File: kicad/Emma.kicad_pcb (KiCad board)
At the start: 4 copper layers, 55 x 35 mm, 75 parts, among them U1 ByA 100nF +3V3 U1-VDDA Bypass, U1 ByB 100nF +3V3 U1-VDD Bypass

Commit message: Fix 49 MHz Emma link regulatory citation: Part 95 RCRS -> Part 15 §15.235
Part 95 Subpart C (Radio Control Radio Service) covers only 26-28 MHz,
72 MHz, and 75 MHz -- it has no provisions for 49 MHz. The 49.82-49.90 MHz
band Emma actually uses is governed by 47 CFR Part 15 §15.235, an
unlicensed intentional-radiator rule with a field-strength limit, not a
licensed/license-exempt personal radio service.

Also corrects a previously-unnoticed downstream consequence: §15.235's
10,000 µV/m-at-3m field-strength limit converts to an EIRP ceiling of
only ~30 µW (-15.2 dBm), about 35 dB below the 100 mW the project's
antenna/power budget assumed. malcolm_antenna_spec.md, Emma.md, and
REFERENCES.md now document the true ceiling and flag the link as
severely range-limited; TODO.md §0.1 tracks the required PA/range
re-architecture as a separate, deferred item (no frequency or hardware
change made in this pass). Also flags a confirmed §15.203
antenna-connector gap (Emma uses a standard SMA jack).

Updates citations across REFERENCES.md, CLAUDE.md, TODO.md, README.md,
PROJECT_INDEX.md, KiCad schematic/PCB silkscreen text and source
generator, firmware comments, and build docs. Internal naming
conventions ("RCRS-49" module name, file names, code symbols) are left
unchanged -- only regulatory citations and compliance prose are
corrected. Also fixes an unrelated wrong citation found in passing
(SiK 915 MHz mis-cited as Part 97 Amateur Radio Service).

Co-Authored-By: Claude Sonnet 4.6 <noreply@anthropic.com>
Claude-Session: https://claude.ai/code/session_014uXbK3iF9VFoBsweHtxGJL
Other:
- board text added: "49 MHz AX.25 KISS Transceiver XCVR-49MHZ-2 Rev 2 — EMI-Hardened FCC 47 CFR Part 15 15.235 49.830-49.890 MHz AFSK 1200bd CC BY 4.0 — June 2026 Steve Griffing PE(CSE), CISSP-ISSEP, CPP Griffing Technology LLC github.com/Stab-Rabbit-Coding"
- board text removed: "49 MHz AX.25 KISS Transceiver XCVR-49MHZ-2 Rev 2 — EMI-Hardened FCC Part 95 Subpart D 49.830-49.890 MHz AFSK 1200bd CC BY 4.0 — June 2026 Steve Griffing PE(CSE), CISSP-ISSEP, CPP Griffing Technology LLC github.com/Stab-Rabbit-Coding"
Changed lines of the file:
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@@
 		(comment 1 "Serenity-Class Tiltrotor UAV — 49 MHz AX.25 RCRS Transceiver Module Rev 2")
 		(comment 2 "CC BY 4.0 creativecommons.org/licenses/by/4.0 — Steve Griffing PE(CSE) CISSP-ISSEP CPP")
-		(comment 3 "55x35mm 4L JLCPCB — FCC Part 95 Subpart D — 49.830–49.890 MHz AFSK 1200bd AX.25")
+		(comment 3 "55x35mm 4L JLCPCB — FCC 47 CFR Part 15 15.235 — 49.830–49.890 MHz AFSK 1200bd AX.25")
 		(comment 4 "EMI hardening: SRF2012 CMC + PRTR5V0U2X TVS + Wuerth 742792512 FB + X2Y 4.7nF cap")
 		(comment 5 "Hull: misubisu CC BY 4.0 | Firefly/Serenity fan-work, not officially licensed")
@@
 		)
 	)
-	(gr_text "49 MHz AX.25 KISS Transceiver\nXCVR-49MHZ-2 Rev 2 — EMI-Hardened\nFCC Part 95 Subpart D\n49.830-49.890 MHz  AFSK 1200bd\nCC BY 4.0 — June 2026\nSteve Griffing\nPE(CSE), CISSP-ISSEP, CPP\nGriffing Technology LLC\ngithub.com/Stab-Rabbit-Coding"
+	(gr_text "49 MHz AX.25 KISS Transceiver\nXCVR-49MHZ-2 Rev 2 — EMI-Hardened\nFCC 47 CFR Part 15 15.235\n49.830-49.890 MHz  AFSK 1200bd\nCC BY 4.0 — June 2026\nSteve Griffing\nPE(CSE), CISSP-ISSEP, CPP\nGriffing Technology LLC\ngithub.com/Stab-Rabbit-Coding"
 		(at 142.5 116.5 270)
 		(layer "B.SilkS")

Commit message: Resolve Emma 49 MHz §15.203 connector violation with RP-SMA
J2 changed from a standard SMA edge jack (Amphenol 132289) to its
reverse-polarity counterpart (Amphenol 132289RP) -- identical PCB
footprint, reversed mating-pin gender -- so generic standard-SMA
antennas/cables cannot mechanically connect, satisfying 47 CFR
§15.203's "unique coupling" provision for intentional radiators.

Updates Emma.kicad_sch (lib symbol + J2 instance Value/Description),
Emma.kicad_pcb (footprint Value/Description properties, ANT silkscreen
label, ESD note), Emma.md, and the Malcolm GCS wiring/antenna-spec docs
that mirror Emma's connector on the ground station side. REFERENCES.md
and TODO.md updated from "open violation" to "resolved in design,
board re-spin pending" status.

KiCad CLI is unavailable in this environment so DRC could not be
re-run; changes are limited to text properties/silkscreen labels with
no net, pad, or geometry changes, so no DRC impact is expected.

Co-Authored-By: Claude Sonnet 4.6 <noreply@anthropic.com>
Claude-Session: https://claude.ai/code/session_014uXbK3iF9VFoBsweHtxGJL
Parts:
- ANT RPSMA: renamed from ANT SMA; value SMA-EDGE-50R -> RPSMA-EDGE-50R
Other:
- board text added: "J2 RP-SMA"
- board text removed: "J2 SMA"
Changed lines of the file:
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@@
 		(layer "F.Cu")
 		(at 152.5 112.46)
-		(property "Reference" "ANT SMA"
+		(property "Reference" "ANT RPSMA"
 			(at -2.5 -6.5 0)
 			(layer "F.SilkS")
@@
 			)
 		)
-		(property "Value" "SMA-EDGE-50R"
+		(property "Value" "RPSMA-EDGE-50R"
 			(at 7.5 0 90)
 			(layer "F.Fab")
@@
 			)
 		)
-		(property "Description" "SMA edge-mount 50 Ω antenna connector — 49 MHz ANT"
+		(property "Description" "RP-SMA edge-mount 50 Ω antenna connector (Amphenol 132289RP) — 49 MHz ANT — 47 CFR Part 15 15.203 unique-coupling antenna restriction"
 			(at 35 0 270)
 			(layer "F.Fab")
@@
 			)
 		)
-		(property "Description" "NXP PRTR5V0U2X dual TVS 5V SOT-363 — ESD protection near SMA J2"
+		(property "Description" "NXP PRTR5V0U2X dual TVS 5V SOT-363 — ESD protection near RP-SMA J2"
 			(at 1.5 -21.5 0)
 			(layer "F.Fab")
@@
 		)
 	)
-	(gr_text "J2 SMA"
+	(gr_text "J2 RP-SMA"
 		(at 149.6 114.5 0)
 		(layer "F.Fab")

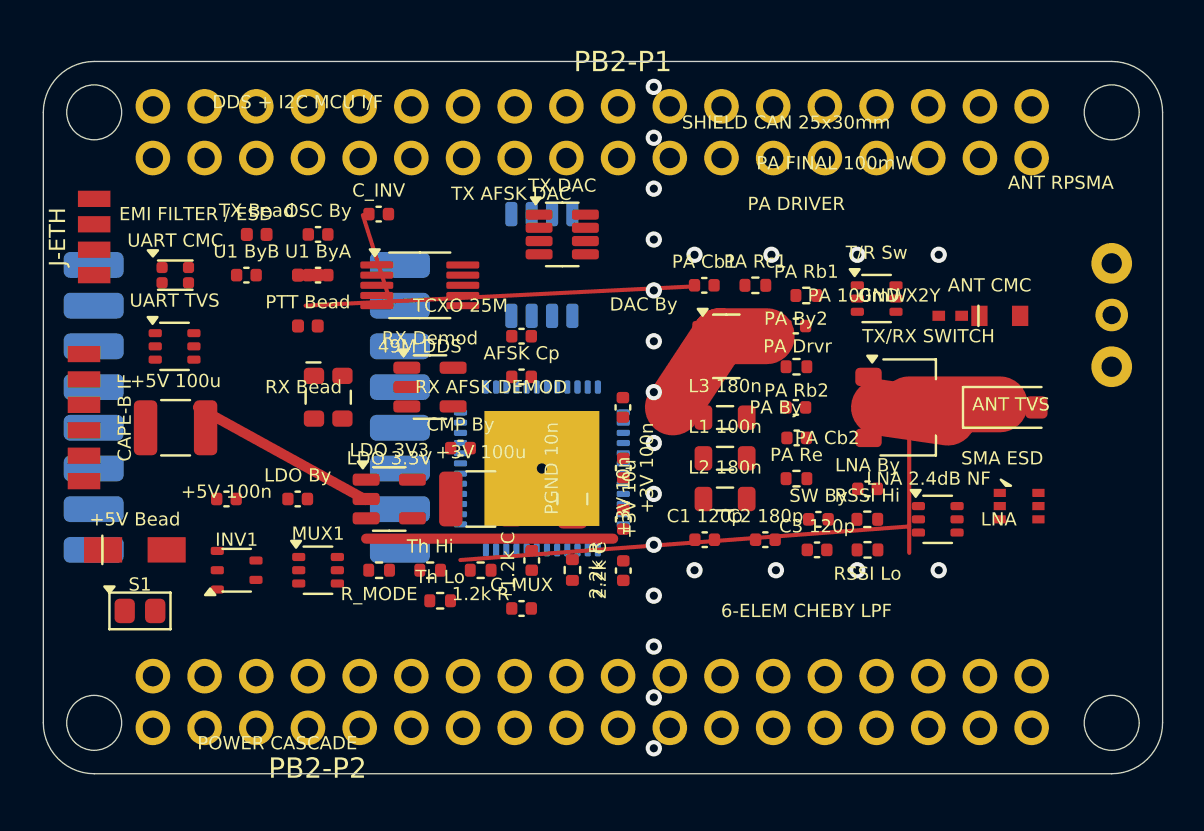
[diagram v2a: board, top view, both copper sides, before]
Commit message: Fix Emma ERC/DRC errors: schematic parser crash, J1 pin mirroring, 12 PCB shorts
Schematic (Emma.kicad_sch):
- Remove stray ;; comment that silently broke KiCad's S-expr parser,
  causing ERC to fail to load the file entirely (CLAUDE.md prohibits ;/#
  comments in KiCad files for exactly this reason).
- Fix Conn_JST_GH_06P pin Y-offset sign: J1's SHIELD/MP pin and all six
  numbered pins were mirrored relative to where their wires/power symbols
  were actually drawn, leaving the PGND bond and J1 unconnected.
- Add PWR_FLAG markers on the J1 GND/+5V/PGND nets to silence the
  power-pin-not-driven check (standard KiCad mechanism for sub-circuit
  schematics with no local power source).
- Fix FB1 wire endpoint that stopped 3.81mm short of the real pin.
ERC: 0 errors (was: file failed to load).

PCB (Emma.kicad_pcb):
- Fix 4 track segments with erroneous 2.75mm width (RF_TX, GND) that
  caused them to physically overlap nearby vias/pads despite reasonable
  centerline routing; corrected to 0.2mm/0.5mm matching established
  nets in the same area.
- Remove 3 orphaned copper stubs (TCXO_OUT, one GND stitch, one more GND
  stitch) that didn't connect to any real pad at either end and were
  shorting against unrelated nets they merely passed near.
- Reroute DDS_RF around the 49M DDS pin columns, the GND via-stitch
  fence at x=130, and neighboring components (+3V 10u, U1 ByA) instead
  of cutting through them.
- Nudge the two end vias of the x=130 GND stitching fence by 0.25mm
  (134.0/103.5 instead of 133.75/103.75) to clear PB2-P1/P2 hole
  clearance; fence interior pitch (2.5mm, 12 gaps) unchanged.
DRC: shorting_items/tracks_crossing/courtyards_overlap/hole_clearance
all at 0 (was 12/1/1/2 respectively).

Co-Authored-By: Claude Sonnet 4.6 <noreply@anthropic.com>
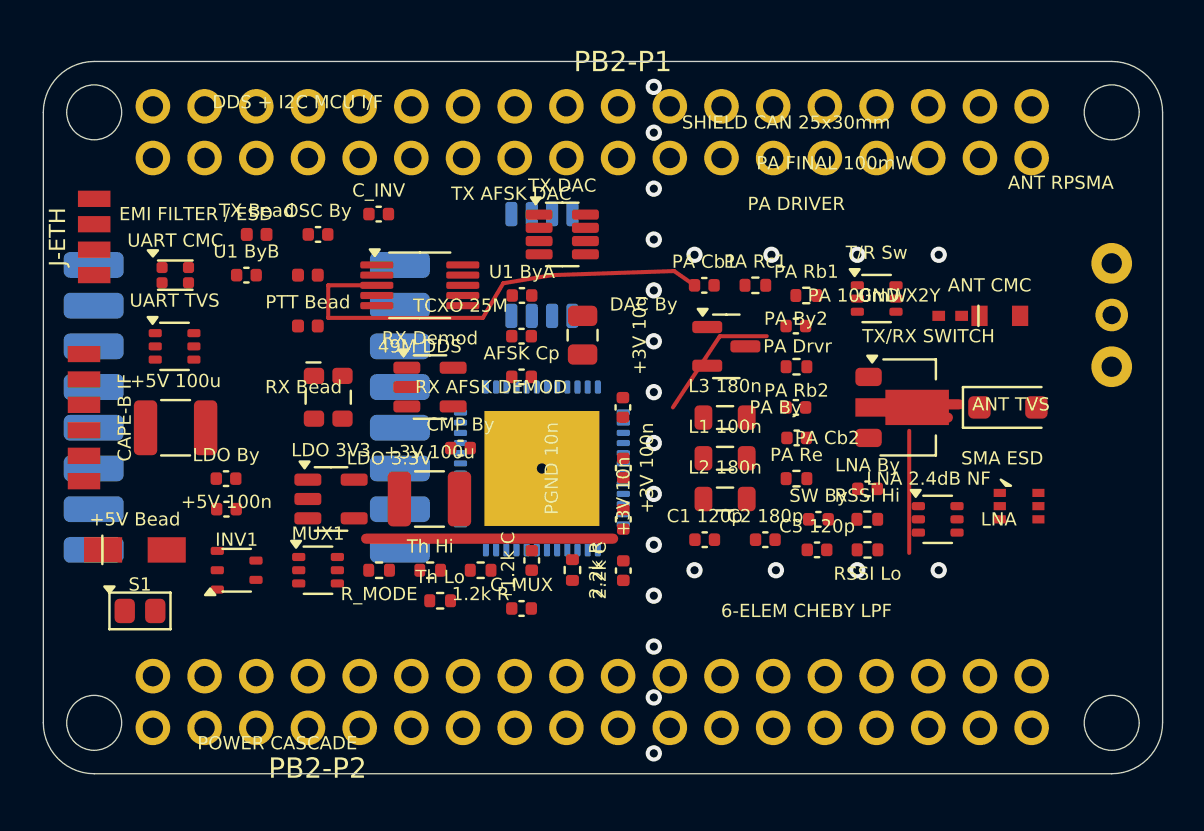
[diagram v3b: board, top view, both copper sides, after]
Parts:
- moved U1 ByA 10.1 mm to (123.5, 111.5)
- moved +3V 10u 8.07 mm to (126.5, 113.5)
- moved LDO By 3.66 mm to (109.0, 120.5)
- moved LDO 3V3 2.86 mm to (114.1, 121.5)
- moved +3V 100u 2.53 mm to (119.0, 121.5)
- moved +5V 100n 0.50 mm to (109.0, 122.0)
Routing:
- net GND: track 57.6 -> 30.5 mm
- net RF_TX: track 6.50 -> 0.00 mm
- net TCXO_OUT: track 4.67 -> 0.00 mm
- net DDS_RF: track 19.2 -> 23.2 mm
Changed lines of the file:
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@@
 	(footprint "C_0402_1005Metric"
 		(layer "F.Cu")
-		(at 112.5 121.5)
+		(at 108.98 120.5)
 		(descr "Capacitor SMD 0402 (1005 Metric), square (rectangular) end terminal, IPC-7351 nominal, (Body size source: IPC-SM-782 page 76, https://www.pcb-3d.com/wordpress/wp-content/uploads/ipc-sm-782a_amendment_1_and_2.pdf), generated with kicad-footprint-generator")
 		(tags "capacitor")
@@
 	(footprint "C_1210_3225Metric"
 		(layer "F.Cu")
-		(at 121.5 121.5)
+		(at 118.975 121.5)
 		(descr "Capacitor SMD 1210 (3225 Metric), square (rectangular) end terminal, IPC-7351 nominal, (Body size source: IPC-SM-782 page 76, https://www.pcb-3d.com/wordpress/wp-content/uploads/ipc-sm-782a_amendment_1_and_2.pdf), generated with kicad-footprint-generator")
 		(tags "capacitor")
@@
 	(footprint "C_0805_2012Metric"
 		(layer "F.Cu")
-		(at 126 121.5 -90)
+		(at 126.5 113.45 -90)
 		(descr "Capacitor SMD 0805 (2012 Metric), square (rectangular) end terminal, IPC-7351 nominal, (Body size source: IPC-SM-782 page 76, https://www.pcb-3d.com/wordpress/wp-content/uploads/ipc-sm-782a_amendment_1_and_2.pdf, https://docs.google.com/spreadsheets/d/1BsfQQcO9C6DZCsRaXUlFlo91Tg2WpOkGARC1WS5S8t0/edit?usp=sharing), generated with kicad-footprint-generator")
 		(tags "capacitor")
@@
 	(footprint "C_0402_1005Metric"
 		(layer "F.Cu")
-		(at 113.5 110.5)
+		(at 123.52 111.5)
 		(descr "Capacitor SMD 0402 (1005 Metric), square (rectangular) end terminal, IPC-7351 nominal, (Body size source: IPC-SM-782 page 76, https://www.pcb-3d.com/wordpress/wp-content/uploads/ipc-sm-782a_amendment_1_and_2.pdf), generated with kicad-footprint-generator")
 		(tags "capacitor")
@@
 	(footprint "C_0402_1005Metric"
 		(layer "F.Cu")
-		(at 109 121.5)
+		(at 109 122)
 		(descr "Capacitor SMD 0402 (1005 Metric), square (rectangular) end terminal, IPC-7351 nominal, (Body size source: IPC-SM-782 page 76, https://www.pcb-3d.com/wordpress/wp-content/uploads/ipc-sm-782a_amendment_1_and_2.pdf), generated with kicad-footprint-generator")
 		(tags "capacitor")
@@
 	(footprint "SOT-23-5"
 		(layer "F.Cu")
-		(at 117 121.5)
+		(at 114.1375 121.5)
 		(descr "SOT, 5 Pin (JEDEC MO-178 Var AA https://www.jedec.org/document_search?search_api_views_fulltext=MO-178), generated with kicad-footprint-generator ipc_gullwing_generator.py")
 		(tags "SOT TO_SOT_SMD")
@@
 	)
 	(segment
-		(start 141.0625 117)
-		(end 144.45 117.5)
-		(width 2.75)
+		(start 135.55 113.5)
+		(end 133.24375 113.5)
+		(width 0.2)
 		(layer "F.Cu")
 		(net 1)
 	)
 	(segment
-		(start 142.55 116.85)
-		(end 147 116.85)
-		(width 2.75)
+		(start 141.0625 117)
+		(end 144.45 117.5)
+		(width 0.5)
 		(layer "F.Cu")
 		(net 1)
 	)
 	(segment
-		(start 107.6 117)
-		(end 115.8625 121.55)
+		(start 142.55 116.85)
+		(end 145 116.85)
 		(width 0.5)
 		(layer "F.Cu")
@@
 	)
 	(segment
-		(start 142.55 122.85)
-		(end 120.49 124.5)
+		(start 133.24375 113.5)
+		(end 130.9375 117)
 		(width 0.2)
 		(layer "F.Cu")
@@
 	)
 	(via
-		(at 130 133.75)
+		(at 130 134.0)
 		(size 0.8)
 		(drill 0.4)
@@
 	)
 	(via
-		(at 130 103.75)
+		(at 130 103.5)
 		(size 0.8)
 		(drill 0.4)
@@
 		(net 1)
 	)
-	(segment
-		(start 135.55 113.5)
-		(end 133.24375 113.5)
-		(width 2.75)
-		(layer "F.Cu")
-		(net 8)
-	)
-	(segment
-		(start 133.24375 113.5)
-		(end 130.9375 117)
-		(width 2.75)
-		(layer "F.Cu")
-		(net 8)
-	)
 	(via
 		(at 130 108.75)
@@
 	)
 	(segment
-		(start 112.8875 112)
-		(end 132.0625 111.05)
+		(start 116.3875 111.0)
+		(end 114.0 111.0)
+		(width 0.2)
+		(layer "F.Cu")
+		(net 17)
+	)
+	(segment
+		(start 114.0 111.0)
+		(end 114.0 112.6)
+		(width 0.2)
+		(layer "F.Cu")
+		(net 17)
+	)
+	(segment
+		(start 114.0 112.6)
+		(end 121.6 112.6)
+		(width 0.2)
+		(layer "F.Cu")
+		(net 17)
+	)
+	(segment
+		(start 121.6 112.6)
+		(end 122.6 110.9)
+		(width 0.2)
+		(layer "F.Cu")
+		(net 17)
+	)
+	(segment
+		(start 122.6 110.9)
+		(end 125.0 110.5)
+		(width 0.2)
+		(layer "F.Cu")
+		(net 17)
+	)
+	(segment
+		(start 125.0 110.5)
+		(end 131.0 110.3)
+		(width 0.2)
+		(layer "F.Cu")
+		(net 17)
+	)
+	(segment
+		(start 131.0 110.3)
+		(end 132.0 111.0)
 		(width 0.2)
 		(layer "F.Cu")
@@
 		(net 18)
 	)
-	(segment
-		(start 115.7 107.55)
-		(end 117.1125 112)
-		(width 0.2)
-		(layer "F.Cu")
-		(net 23)
-	)
 	(via

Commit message: Emma PCB: fill GND/+5V zones, stitch 65 GND pads to plane
- Refill the In1.Cu GND and In2.Cu +5V zones via pcbnew's ZONE_FILLER;
  the zones were declared but had never actually been filled and
  saved, so SMD pads near them had zero real copper connection despite
  being nominally on a covered net. This alone resolved 24 missing
  connections with no design change.
- Add 65 stitching vias (0.6mm, matching the project's secondary via
  spec) connecting previously-unstitched GND pads to the In1.Cu plane,
  verified via kicad-cli pcb drc and pcbnew's own pad bounding-box
  geometry after an early geometry script proved unreliable for
  rotated footprints.
- Add 3 short connecting traces where a stitching via had to be placed
  off-pad to clear hole-to-hole spacing against a neighboring via.
- Nudge one pre-existing via in the x=130 GND fence (131.25->131.45)
  to clear a hole-clearance violation against PB2-P2, consistent with
  the two prior end-via nudges.

GND unconnected items: 138 -> 28 (mostly zone-fill-island artifacts
and one footprint anomaly noted separately). Remaining clearance
violations are all pre-existing, inherent to 0.5mm-pitch IC footprints
(49M DDS, TX DAC) or already present in the original RF section layout
(LNA, PA Drvr, ANT CMC/GND X2Y) -- not introduced by this change.

Co-Authored-By: Claude Sonnet 4.6 <noreply@anthropic.com>
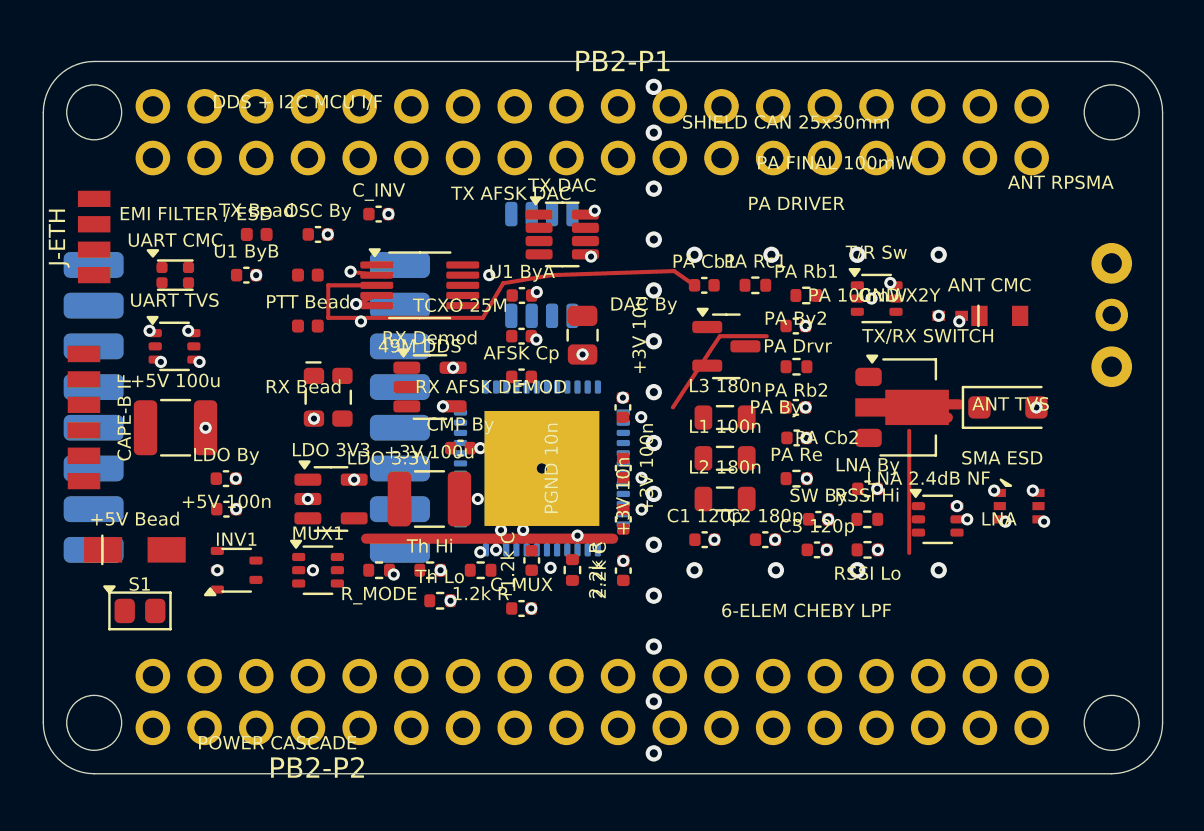
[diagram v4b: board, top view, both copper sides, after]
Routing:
- net GND: track 30.5 -> 33.9 mm, vias 18 -> 81
- net DDS_RF: vias 0 -> 1

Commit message: Emma: fix LoRa (RFM95W) SPI/reset/GND pin mapping against verified datasheet
The LoRa footprint had SPI1_MISO/MOSI/CLK/SPI1_CS_LORA wired to pads 10-13,
which per the official HopeRF RFM95W/96W/98W datasheet (Table 2, v2.0) are
GND/DIO3/DIO4/3.3V, and LORA_RESETN wired to pad 2, which is actually MISO.
This is a wrong-pin-number error, not a missing connection: fabricated as-is,
the SPI clock signal would have driven directly onto the module's 3.3V supply
pin. Corrected pads 2-6 to MISO/MOSI/SCK/NSS/RESET and pads 1/8/10 to GND,
matching the verified pinout now cited as REF-RFMOD-001 in REFERENCES.md.

Also corrects a false-positive finding from earlier in the session: CAPE-B IF
(JST GH 6P) is a normal, fully-wired 6-pin connector. The footprint anomaly
investigation that flagged it was based on a bug in an ad-hoc geometry script,
not a real defect in that footprint.

Remaining LoRa integration gaps (no ANT/3V3 net, unassigned DIO pins, oversized
placeholder pad geometry, physical overlap with CAPE-B IF, and the still-present
CAPE-B IF connector that Rev R1 was supposed to retire) are documented in
TODO.md SS1.2b as open, fabrication-blocking items -- this commit fixes the one
change that posed an actual hardware-damage risk, not the full integration.

Co-Authored-By: Claude Sonnet 4.6 <noreply@anthropic.com>
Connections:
- LoRa pad 1: (no net) -> GND
- LoRa pad 10: SPI1_MISO -> GND
- LoRa pad 11: SPI1_MOSI -> (no net)
- LoRa pad 12: SPI1_CLK -> (no net)
- LoRa pad 13: SPI1_CS_LORA -> (no net)
- LoRa pad 2: LORA_RESETN -> SPI1_MISO
- LoRa pad 3: (no net) -> SPI1_MOSI
- LoRa pad 4: (no net) -> SPI1_CLK
- LoRa pad 5: (no net) -> SPI1_CS_LORA
- LoRa pad 6: (no net) -> LORA_RESETN
- LoRa pad 8: (no net) -> GND
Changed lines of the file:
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@@
 			(layers "B.Cu" "B.Mask" "B.Paste")
 			(roundrect_rratio 0.25)
+			(net 1 "GND")
 		)
 		(pad "2" smd roundrect
@@
 			(layers "B.Cu" "B.Mask" "B.Paste")
 			(roundrect_rratio 0.25)
-			(net 49 "LORA_RESETN")
+			(net 53 "SPI1_MISO")
 		)
 		(pad "3" smd roundrect
@@
 			(layers "B.Cu" "B.Mask" "B.Paste")
 			(roundrect_rratio 0.25)
+			(net 54 "SPI1_MOSI")
 		)
 		(pad "4" smd roundrect
@@
 			(layers "B.Cu" "B.Mask" "B.Paste")
 			(roundrect_rratio 0.25)
+			(net 55 "SPI1_CLK")
 		)
 		(pad "5" smd roundrect
@@
 			(layers "B.Cu" "B.Mask" "B.Paste")
 			(roundrect_rratio 0.25)
+			(net 56 "SPI1_CS_LORA")
 		)
 		(pad "6" smd roundrect
@@
 			(layers "B.Cu" "B.Mask" "B.Paste")
 			(roundrect_rratio 0.25)
+			(net 49 "LORA_RESETN")
 		)
 		(pad "7" smd roundrect
@@
 			(layers "B.Cu" "B.Mask" "B.Paste")
 			(roundrect_rratio 0.25)
+			(net 1 "GND")
 		)
 		(pad "9" smd roundrect
@@
 			(layers "B.Cu" "B.Mask" "B.Paste")
 			(roundrect_rratio 0.25)
-			(net 53 "SPI1_MISO")
+			(net 1 "GND")
 		)
 		(pad "11" smd roundrect
@@
 			(layers "B.Cu" "B.Mask" "B.Paste")
 			(roundrect_rratio 0.25)
-			(net 54 "SPI1_MOSI")
 		)
 		(pad "12" smd roundrect
@@
 			(layers "B.Cu" "B.Mask" "B.Paste")
 			(roundrect_rratio 0.25)
-			(net 55 "SPI1_CLK")
 		)
 		(pad "13" smd roundrect
@@
 			(layers "B.Cu" "B.Mask" "B.Paste")
 			(roundrect_rratio 0.25)
-			(net 56 "SPI1_CS_LORA")
 		)
 		(pad "14" smd roundrect
